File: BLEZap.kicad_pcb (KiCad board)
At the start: 2 copper layers, 38.1 x 22.9 mm, 11 parts, among them P1 PRG_HEADER, P2 INPUT_HEADER, P3 CONN_01X02, Q1 IRLML6344, U1 Core51822B

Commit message: Core51822 Fix
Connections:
- U1 pad 10: Net-(U1-Pad10) -> (no net)
- U1 pad 13: Net-(U1-Pad13) -> (no net)
- U1 pad 17: Net-(U1-Pad17) -> (no net)
- U1 pad 18: Net-(U1-Pad18) -> (no net)
- U1 pad 19: Net-(U1-Pad19) -> (no net)
- U1 pad 2: Net-(U1-Pad2) -> (no net)
- U1 pad 20: Net-(U1-Pad20) -> (no net)
- U1 pad 21: Net-(U1-Pad21) -> (no net)
- U1 pad 22: Net-(U1-Pad22) -> (no net)
- U1 pad 25: Net-(U1-Pad25) -> (no net)
- U1 pad 26: Net-(U1-Pad26) -> (no net)
- U1 pad 27: Net-(U1-Pad27) -> (no net)
- U1 pad 28: Net-(U1-Pad28) -> (no net)
- U1 pad 3: Net-(U1-Pad3) -> (no net)
- U1 pad 30: /SWDIO -> (no net)
- U1 pad 31: /SWCLK -> /SWDIO
- U1 pad 32: (no net) -> /SWCLK
- U1 pad 33: Net-(U1-Pad33) -> (no net)
- U1 pad 34: Net-(U1-Pad34) -> (no net)
- U1 pad 35: Net-(U1-Pad35) -> (no net)
- U1 pad 36: Net-(U1-Pad36) -> (no net)
- U1 pad 4: Net-(U1-Pad4) -> (no net)
- U1 pad 5: Net-(U1-Pad5) -> (no net)
- U1 pad 6: Net-(U1-Pad6) -> (no net)
- U1 pad 7: Net-(U1-Pad7) -> (no net)
- U1 pad 8: Net-(U1-Pad8) -> (no net)
- U1 pad 9: Net-(U1-Pad9) -> (no net)
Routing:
- net /SWCLK: track 27.9 -> 29.2 mm
- net /CFG_BTN: track 16.7 -> 17.9 mm
- net /SWDIO: track 29.3 -> 29.9 mm
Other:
- net class Default: trace_width 0.1524 -> 0.254

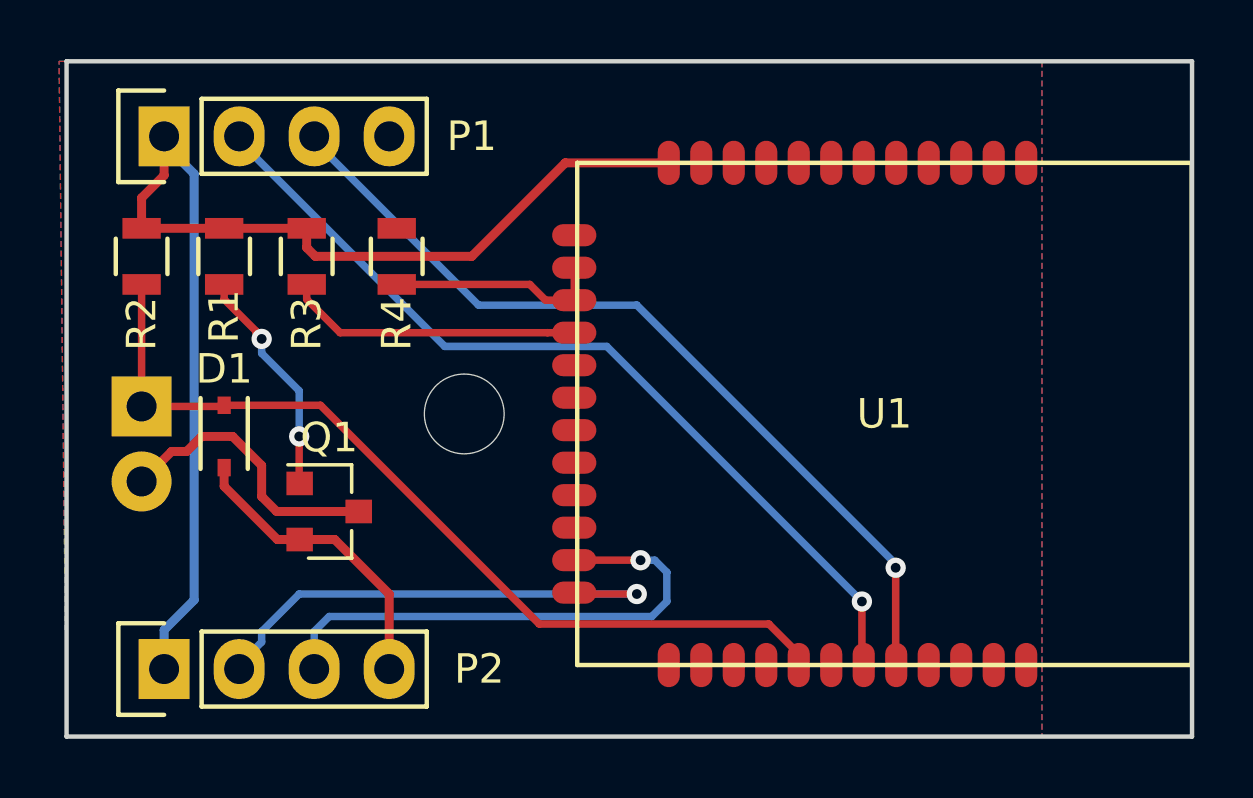
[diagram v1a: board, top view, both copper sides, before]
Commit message: Protection Diode
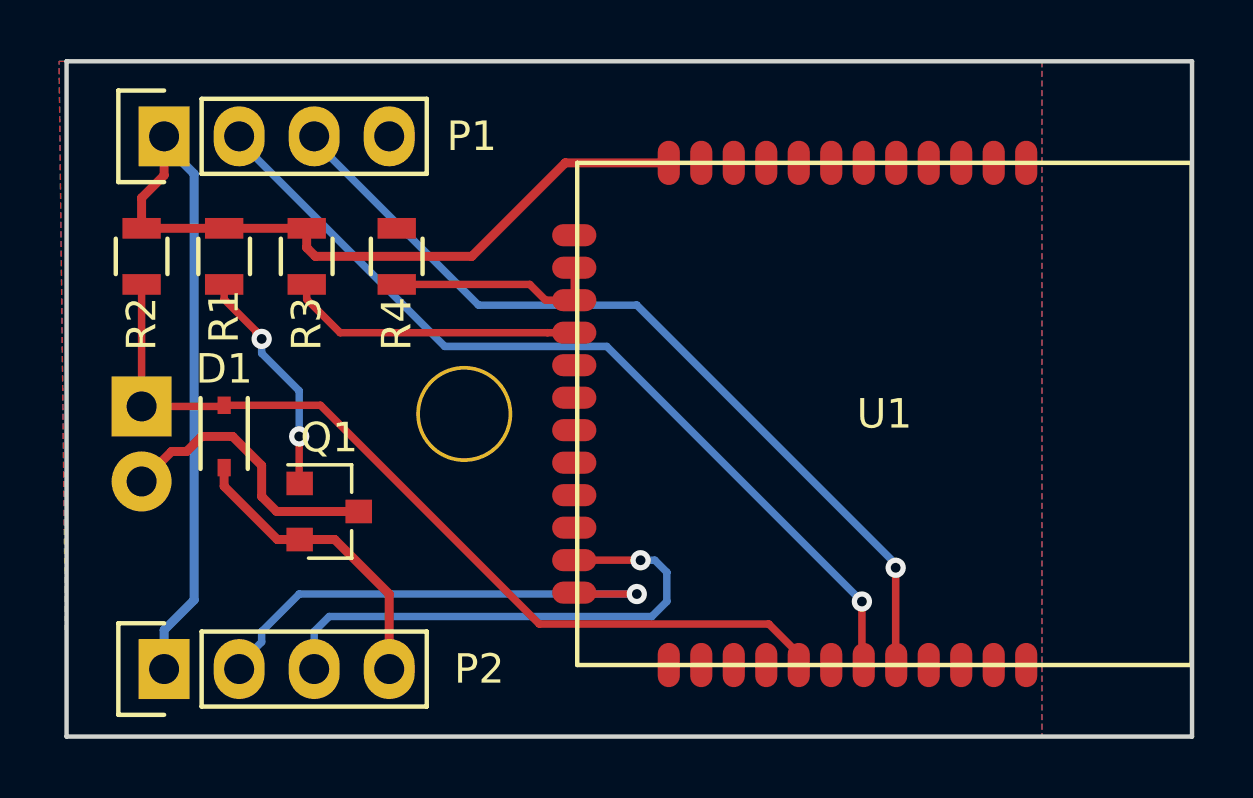
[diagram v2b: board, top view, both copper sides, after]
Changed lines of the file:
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@@
     (mod_text_size 1 1)
     (mod_text_width 0.15)
-    (pad_size 1.524 1.524)
-    (pad_drill 0.762)
+    (pad_size 3.25 3.25)
+    (pad_drill 3)
     (pad_to_mask_clearance 0.2)
     (aux_axis_origin 0 0)
@@
     (fp_circle (center 0 0) (end 2.7 0) (layer Cmts.User) (width 0.15))
     (fp_circle (center 0 0) (end 2.95 0) (layer F.CrtYd) (width 0.05))
-    (pad 1 np_thru_hole circle (at 0 0) (size 2.7 2.7) (drill 2.7) (layers *.Cu *.Mask))
+    (pad "" np_thru_hole circle (at 0 0) (size 3.25 3.25) (drill 3) (layers *.Cu *.Mask))
   )
   (gr_line (start 114.3 99.06) (end 76.2 99.06) (angle 90) (layer Edge.Cuts) (width 0.15))

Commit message: Version 2
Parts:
- removed Q1: IRLML6344, TO_SOT_Packages_SMD:SOT-23
- removed R1: 100R, Resistors_SMD:R_0805
- removed the REF** at (89.7, 88.1)
- added ?: 1pin, Connectors:1pin, F.Cu at (88.4, 87.6)
- added D2: 1N5819, Diodes_SMD:D_0805, F.Cu at (84.6, 91.7)
- added REF**: VIA_13MIL, KevinLibrary:VIA_13MIL, F.Cu at (83.3, 89.2)
- added REF**: VIA_13MIL, KevinLibrary:VIA_13MIL, F.Cu at (106.9, 84.8)
- added REF**: VIA_13MIL, KevinLibrary:VIA_13MIL, F.Cu at (99.3, 91.7)
- added REF**: VIA_13MIL, KevinLibrary:VIA_13MIL, F.Cu at (100.3, 77.5)
- added REF**: VIA_13MIL, KevinLibrary:VIA_13MIL, F.Cu at (78.7, 93.2)
- added REF**: VIA_13MIL, KevinLibrary:VIA_13MIL, F.Cu at (89.9, 95.5)
- added REF**: VIA_13MIL, KevinLibrary:VIA_13MIL, F.Cu at (99.6, 86.1)
- added REF**: VIA_13MIL, KevinLibrary:VIA_13MIL, F.Cu at (106.2, 91.2)
- added U2: MP1584_MOD, KevinLibrary:MP1584_MOD_ALL_UNDER, F.Cu at (100.6, 87.6)
- U1: moved to B.Cu
- moved R3 2.29 mm to (82.0, 82.8)
- moved R4 2.29 mm to (85.1, 82.8)
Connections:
- P1 pad 4: GNDD -> GND
- P2 pad 1: VDD -> /CFG_BTN
- P2 pad 2: /RELAY -> +24V
- P2 pad 3: /CFG_BTN -> /RELAY
- P3 pad 2: GNDD -> GND
- R4 pad 1: GNDD -> GND
- U1 pad 1: GNDD -> GND
- U1 pad 11: GNDD -> GND
- U1 pad 24: /RELAY -> Net-(D2-Pad2)
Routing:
- net Net-(D2-Pad2): track 0.00 -> 21.3 mm, vias 0 -> 1
- net Net-(R3-Pad2): track 10.0 -> 27.3 mm, vias 0 -> 1
- net +24V: track 0.00 -> 15.1 mm
- net /RELAY: track 16.9 -> 4.03 mm, vias 1 -> 0
- net /CFG_BTN: track 17.9 -> 28.3 mm
- net GNDD: track 9.65 -> 0.00 mm
- net Net-(R4-Pad2): track 7.33 -> 16.1 mm, vias 0 -> 1
- net Net-(Q1-Pad1): track 7.79 -> 0.00 mm, vias 2 -> 0
- net VDD: track 42.5 -> 47.7 mm, vias 0 -> 1
- net /SWCLK: track 29.2 -> 24.3 mm
- net /SWDIO: track 29.9 -> 26.5 mm
- net GND: track 10.3 -> 8.01 mm, vias 0 -> 1
- net Net-(D1-Pad1): track 30.3 -> 32.3 mm, vias 0 -> 1
- added copper zone on B.Cu, net GND
- added copper zone on F.Cu, net GND
- removed copper zone on B.Cu, net GNDD
- removed copper zone on F.Cu, net GNDD

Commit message: Fix MP1584
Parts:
- moved REF** 9.84 mm to (90.9, 80.4)
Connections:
- U2 pad 1: VDD -> GND
- U2 pad 4: GND -> VDD
- U2 pad 5: +24V -> GND
- U2 pad 8: GND -> +24V
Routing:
- net +24V: track 15.1 -> 28.1 mm
- net VDD: track 47.7 -> 59.5 mm

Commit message: LP Filter
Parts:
- removed the REF** at (83.3, 89.2)
- added C1: .1uF, Capacitors_SMD:C_0805, F.Cu at (81.7, 88.9)
- added R1: 10R4, Resistors_SMD:R_0805, F.Cu at (78.9, 82.7)
- R2, R3, R4: value 10R3 -> 10R4
- moved D1 2.42 mm to (83.9, 89.0)
- moved R2 2.41 mm to (81.2, 82.8)
- moved D2 1.73 mm to (86.0, 92.7)
- moved R3 1.27 mm to (83.3, 82.8)
- moved R4 0.63 mm to (85.7, 82.8)
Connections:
- D1 pad 1: Net-(D1-Pad1) -> Net-(C1-Pad1)
- P3 pad 1: Net-(D1-Pad1) -> Net-(P3-Pad1)
- R2 pad 2: Net-(D1-Pad1) -> Net-(C1-Pad1)
- U1 pad 29: Net-(D1-Pad1) -> Net-(C1-Pad1)
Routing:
- net Net-(C1-Pad1): track 0.00 -> 33.2 mm, vias 0 -> 1
- net Net-(D1-Pad1): track 32.3 -> 0.00 mm, vias 1 -> 0
- net Net-(P3-Pad1): track 0.00 -> 4.24 mm
- net Net-(R3-Pad2): track 27.3 -> 24.6 mm
- net GND: track 8.07 -> 6.46 mm
- net /CFG_BTN: track 28.3 -> 29.8 mm
- net Net-(D2-Pad2): track 21.3 -> 20.3 mm
- net VDD: track 59.5 -> 58.7 mm
- net Net-(R4-Pad2): track 16.1 -> 15.5 mm
